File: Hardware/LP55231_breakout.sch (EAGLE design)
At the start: 29 parts, among them J1 To micro, J2 USER LED, J3 USER LED, J4 USER LED, U1 LP55231WQFN

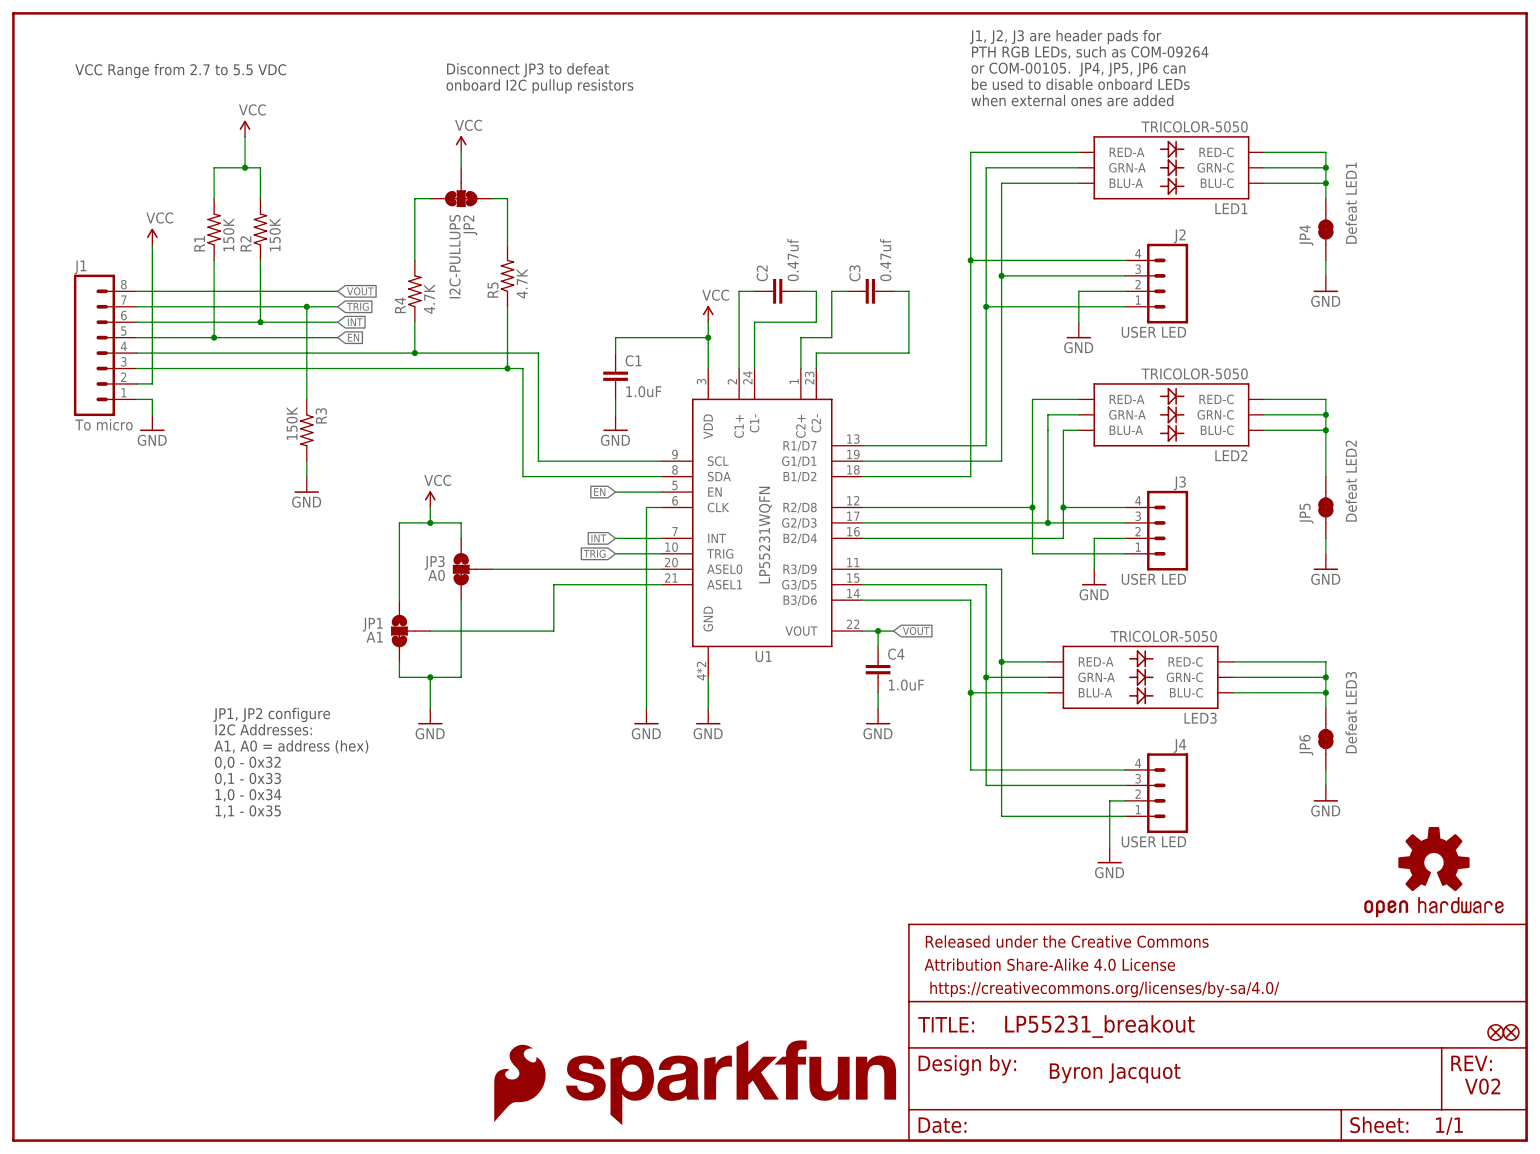
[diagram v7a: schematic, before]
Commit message: Checklist updates for proto round 2.
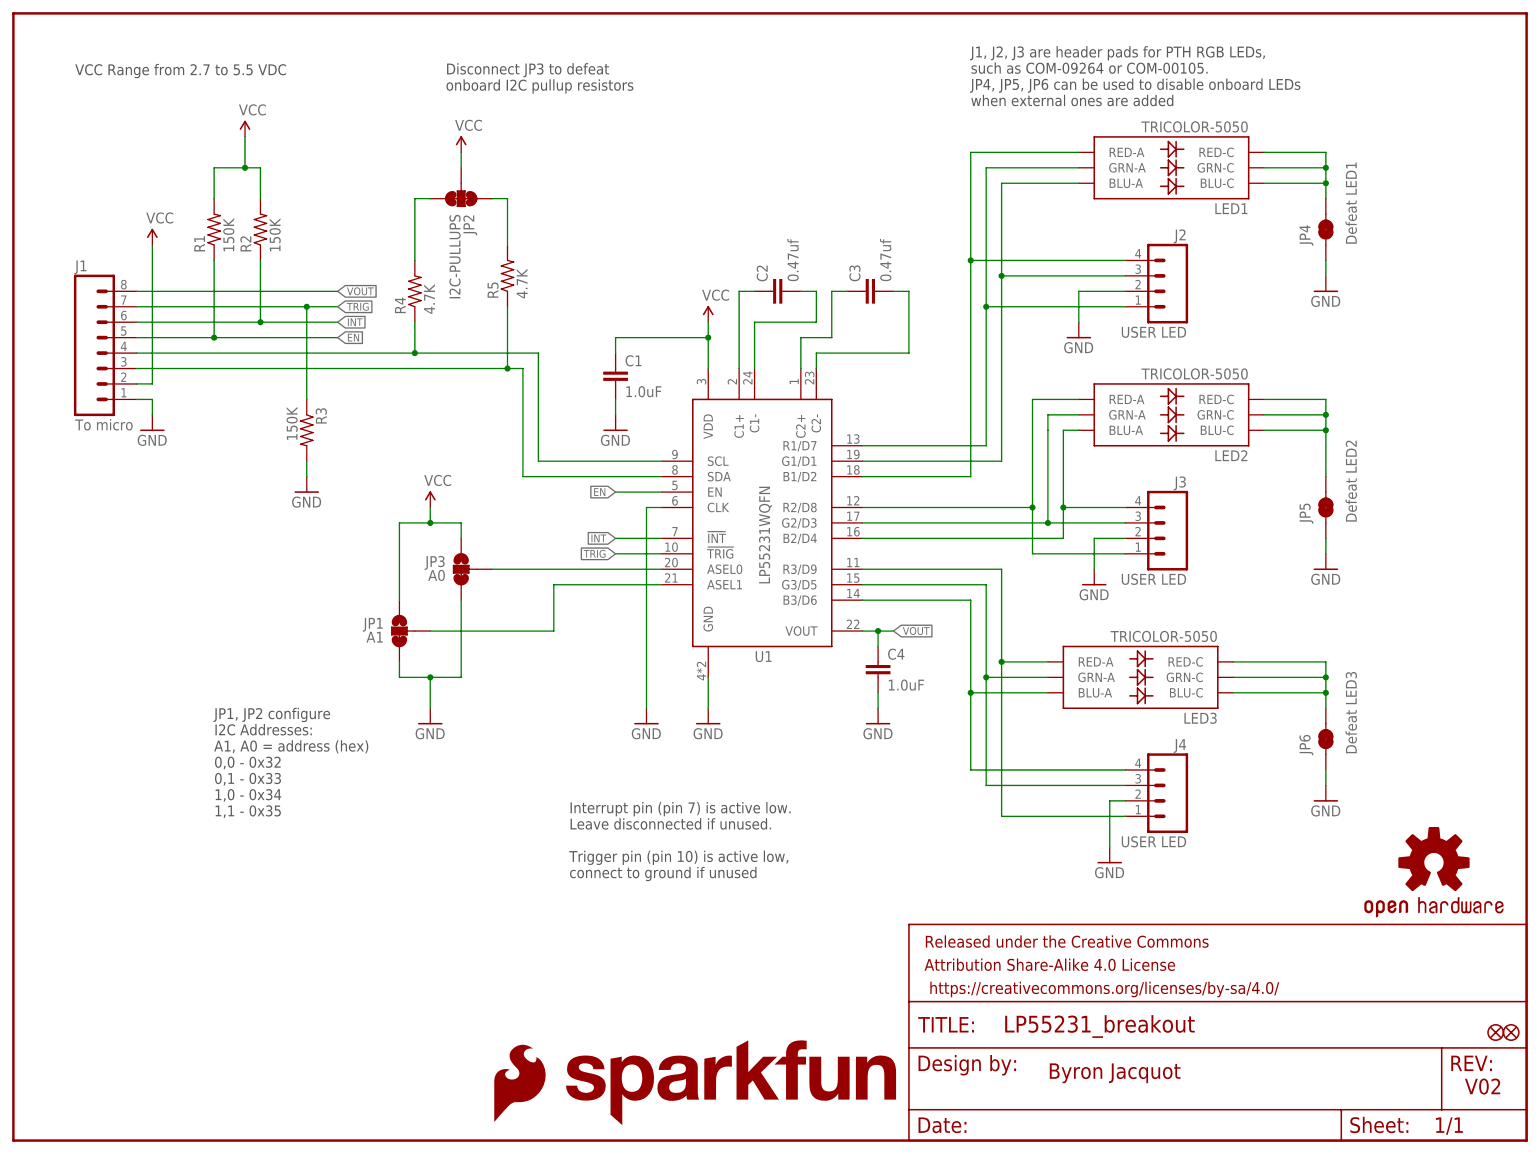
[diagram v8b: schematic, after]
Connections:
- net INT: now also U1.!INT; no longer U1.INT
- net TRIG: now also U1.!TRIG; no longer U1.TRIG
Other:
- note added: "Interrupt pin (pin 7) is active low. Leave disconnected if unused. Trigger pin (pin 10) is active low, connect to ground if unused"
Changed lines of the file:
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@@
 1,0 - 0x34
 1,1 - 0x35</text>
-<text x="157.48" y="170.18" size="1.778" layer="97" font="vector">J1, J2, J3 are header pads for
-PTH RGB LEDs, such as COM-09264
-or COM-00105.  JP4, JP5, JP6 can
-be used to disable onboard LEDs
+<text x="157.48" y="170.18" size="1.778" layer="97" font="vector">J1, J2, J3 are header pads for PTH RGB LEDs,
+such as COM-09264 or COM-00105.
+JP4, JP5, JP6 can be used to disable onboard LEDs
 when external ones are added</text>
 <text x="71.12" y="172.72" size="1.778" layer="97" font="vector">Disconnect JP3 to defeat
 onboard I2C pullup resistors</text>
+<text x="91.44" y="43.18" size="1.778" layer="97" font="vector">Interrupt pin (pin 7) is active low.
+Leave disconnected if unused.
+Trigger pin (pin 10) is active low,
+connect to ground if unused</text>
 </plain>
 <instances>
@@
 <net name="INT" class="0">
 <segment>
-<pinref part="U1" gate="G$1" pin="INT"/>
+<pinref part="U1" gate="G$1" pin="!INT"/>
 <wire x1="106.68" y1="99.06" x2="99.06" y2="99.06" width="0.1524" layer="91"/>
 <label x="99.06" y="99.06" size="1.27" layer="95" rot="R180" xref="yes"/>
@@
 <net name="TRIG" class="0">
 <segment>
-<pinref part="U1" gate="G$1" pin="TRIG"/>
+<pinref part="U1" gate="G$1" pin="!TRIG"/>
 <wire x1="106.68" y1="96.52" x2="99.06" y2="96.52" width="0.1524" layer="91"/>
 <label x="99.06" y="96.52" size="1.27" layer="95" rot="R180" xref="yes"/>
